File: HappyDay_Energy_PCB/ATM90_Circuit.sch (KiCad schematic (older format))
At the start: 34 parts

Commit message: sacrificial draft of power section / HappyDay Energy Monitor Schematic
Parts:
- added L? (x2): L_Core_Ferrite_Small, symbol L_Core_Ferrite_Small
- added U?: Si8655_QSOP-16, QSOP-16, symbol Si8655_QSOP-16
- C? (x10): PN (none) -> C
- C?: value C -> 18p; PN (none) -> c
- C? (x3): value C -> 18p; PN (none) -> C
- J? (x4): PN (none) -> X
- M? (x2): PN (none) -> ATM90E26-YU-RCT-ND
- Y? (x2): PN (none) -> 535-9865-1-ND
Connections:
- net labels added: 3.3V_AVDD, GNDA, GNDREF
- net labels removed: AGND
- wire segments 156 -> 173
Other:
- note added: "ATM90e26 Power"
- moved on the sheet: C?, Y?

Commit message: evolved schematic
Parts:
- removed U?: Si8655_QSOP-16, QSOP-16, symbol Si8655_QSOP-16
- added U?: Si8655, QSOP-16, symbol Si8655
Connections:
- net labels added: +3.3VA, 5V_UNREG, CS0_ATM, CS0_MCU, CS1_ATM, CS1_MCU, GNDPWR, MISO_ATM, MISO_MCU, MOSI_ATM, MOSI_MCU, SCLK_ATM, SCLK_MCU
- net labels removed: CS_0, CS_1, MISO, MOSI, SCLK
- wire segments 173 -> 187
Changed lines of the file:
@@
 	3500 4800 3200 4800
 Text GLabel 3500 4900 2    60   Input ~ 0
-CS_0
+CS0_ATM
 Wire Wire Line
 	3500 4900 3200 4900
@@
 	3500 4600 3200 4600
 Text GLabel 3500 4600 2    60   Input ~ 0
-MOSI
+MOSI_ATM
 Text GLabel 3500 4700 2    60   Output ~ 0
-MISO
+MISO_ATM
 Text GLabel 3500 4800 2    60   Input ~ 0
-SCLK
+SCLK_ATM
 $Comp
 L ATM90E26_ATM90E26 M?
@@
 	7550 4950 7250 4950
 Text GLabel 7550 5050 2    60   Input ~ 0
-CS_1
+CS1_ATM
 Wire Wire Line
 	7550 5050 7250 5050
@@
 	7550 4750 7250 4750
 Text GLabel 7550 4750 2    60   Input ~ 0
-MOSI
+MOSI_ATM
 Text GLabel 7550 4850 2    60   Output ~ 0
-MISO
+MISO_ATM
 Text GLabel 7550 4950 2    60   Input ~ 0
-SCLK
+SCLK_ATM
 $Comp
 L Crystal_Small Y?
@@
 $EndComp
 Text GLabel 10050 5700 3    60   Input ~ 0
-MISO
+MISO_MCU
 Wire Wire Line
 	10050 5700 10050 5500
 Text GLabel 9950 5700 3    60   Output ~ 0
-MOSI
+MOSI_MCU
 Wire Wire Line
 	9950 5500 9950 5700
 Text GLabel 9850 5700 3    60   Output ~ 0
-SCLK
+SCLK_MCU
 Wire Wire Line
 	9850 5700 9850 5500
@@
 Wire Wire Line
 	9250 4350 9250 4550
-$Comp
-L GNDD #PWR?
-U 1 1 5A131861
-P 9150 5700
-F 0 "#PWR?" H 9150 5450 50  0001 C CNN
-F 1 "GNDD" H 9150 5575 50  0000 C CNN
-F 2 "" H 9150 5700 50  0001 C CNN
-F 3 "" H 9150 5700 50  0001 C CNN
-	1    9150 5700
-	1    0    0    -1
-$EndComp
 Wire Wire Line
 	9150 5700 9150 5500
 Text GLabel 9650 4400 1    60   Output ~ 0
-CS_1
+CS1_MCU
 Wire Wire Line
 	9650 4400 9650 4550
 Text GLabel 9750 4400 1    60   Output ~ 0
-CS_0
+CS0_MCU
 Wire Wire Line
 	9750 4400 9750 4550
-$Comp
-L Si8655_QSOP-16 U?
-U 1 1 5A1484DC
-P 7200 1750
-F 0 "U?" H 7850 900 60  0000 C CNN
-F 1 "Si8655_QSOP-16" H 7850 1900 60  0000 C CNN
-F 2 "QSOP-16" H 8400 1990 60  0001 C CNN
-F 3 "" H 7200 1750 60  0000 C CNN
-	1    7200 1750
-	1    0    0    -1
-$EndComp
 Text HLabel 1050 1350 1    60   Input ~ 12
 3.3V_AVDD
@@
 Wire Wire Line
 	1050 1450 1050 1350
-$Comp
-L +3.3V #PWR?
-U 1 1 5A14FD34
-P 600 1250
-F 0 "#PWR?" H 600 1100 50  0001 C CNN
-F 1 "+3.3V" H 600 1390 50  0000 C CNN
-F 2 "" H 600 1250 50  0001 C CNN
-F 3 "" H 600 1250 50  0001 C CNN
-	1    600  1250
-	1    0    0    -1
-$EndComp
 Wire Wire Line
 	600  1250 600  1450
 Wire Wire Line
 	600  1450 700  1450
-$Comp
-L +3.3V #PWR?
-U 1 1 5A14FF70
-P 850 4200
-F 0 "#PWR?" H 850 4050 50  0001 C CNN
-F 1 "+3.3V" H 850 4340 50  0000 C CNN
-F 2 "" H 850 4200 50  0001 C CNN
-F 3 "" H 850 4200 50  0001 C CNN
-	1    850  4200
-	1    0    0    -1
-$EndComp
-$Comp
-L +3.3V #PWR?
-U 1 1 5A14FFE7
-P 2600 3650
-F 0 "#PWR?" H 2600 3500 50  0001 C CNN
-F 1 "+3.3V" H 2600 3790 50  0000 C CNN
-F 2 "" H 2600 3650 50  0001 C CNN
-F 3 "" H 2600 3650 50  0001 C CNN
-	1    2600 3650
-	1    0    0    -1
-$EndComp
-$Comp
-L +3.3V #PWR?
-U 1 1 5A150082
-P 6650 3750
-F 0 "#PWR?" H 6650 3600 50  0001 C CNN
-F 1 "+3.3V" H 6650 3890 50  0000 C CNN
-F 2 "" H 6650 3750 50  0001 C CNN
-F 3 "" H 6650 3750 50  0001 C CNN
-	1    6650 3750
-	1    0    0    -1
-$EndComp
-$Comp
-L +3.3V #PWR?
-U 1 1 5A15011D
-P 5000 4400
-F 0 "#PWR?" H 5000 4250 50  0001 C CNN
-F 1 "+3.3V" H 5000 4540 50  0000 C CNN
-F 2 "" H 5000 4400 50  0001 C CNN
-F 3 "" H 5000 4400 50  0001 C CNN
-	1    5000 4400
-	1    0    0    -1
-$EndComp
-$Comp
-L +3.3V #PWR?
-U 1 1 5A150290
-P 9250 4350
-F 0 "#PWR?" H 9250 4200 50  0001 C CNN
-F 1 "+3.3V" H 9250 4490 50  0000 C CNN
-F 2 "" H 9250 4350 50  0001 C CNN
-F 3 "" H 9250 4350 50  0001 C CNN
-	1    9250 4350
-	1    0    0    -1
-$EndComp
-$Comp
-L +3.3V #PWR?
-U 1 1 5A150532
-P 7050 1550
-F 0 "#PWR?" H 7050 1400 50  0001 C CNN
-F 1 "+3.3V" H 7050 1690 50  0000 C CNN
-F 2 "" H 7050 1550 50  0001 C CNN
-F 3 "" H 7050 1550 50  0001 C CNN
-	1    7050 1550
-	1    0    0    -1
-$EndComp
-Wire Wire Line
-	7200 1750 7050 1750
-Wire Wire Line
-	7050 1750 7050 1550
 $Comp
 L GNDD #PWR?
 U 1 1 5A150691
-P 7200 2600
-F 0 "#PWR?" H 7200 2350 50  0001 C CNN
-F 1 "GNDD" H 7200 2475 50  0000 C CNN
-F 2 "" H 7200 2600 50  0001 C CNN
-F 3 "" H 7200 2600 50  0001 C CNN
-	1    7200 2600
-	1    0    0    -1
-$EndComp
-Wire Wire Line
-	7200 2600 7200 2450
-Wire Wire Line
-	7200 1850 6050 1850
-Wire Wire Line
-	6050 1850 6050 2000
-$Comp
-L GNDD #PWR?
-U 1 1 5A1508DF
-P 6050 2000
-F 0 "#PWR?" H 6050 1750 50  0001 C CNN
-F 1 "GNDD" H 6050 1875 50  0000 C CNN
-F 2 "" H 6050 2000 50  0001 C CNN
-F 3 "" H 6050 2000 50  0001 C CNN
-	1    6050 2000
-	1    0    0    -1
-$EndComp
+P 9000 2600
+F 0 "#PWR?" H 9000 2350 50  0001 C CNN
+F 1 "GNDD" H 9000 2475 50  0000 C CNN
+F 2 "" H 9000 2600 50  0001 C CNN
+F 3 "" H 9000 2600 50  0001 C CNN
+	1    9000 2600
+	1    0    0    -1
+$EndComp
+Wire Wire Line
+	9000 2400 9000 2600
 Text HLabel 1750 1300 1    60   Input ~ 0
 GNDA
@@
 Wire Notes Line
 	2650 2450 2650 500
+Text GLabel 9150 1900 2    60   Output ~ 0
+SCLK_ATM
+Wire Wire Line
+	8850 1900 9150 1900
+Wire Wire Line
+	8850 1700 9000 1700
+Wire Wire Line
+	9000 1550 9000 1800
+Wire Wire Line
+	8850 2400 9000 2400
+Text GLabel 9150 2000 2    60   Output ~ 0
+MOSI_ATM
+Wire Wire Line
+	9150 2000 8850 2000
+Text GLabel 9150 2100 2    60   Output ~ 0
+CS0_ATM
+Wire Wire Line
+	9150 2100 8850 2100
+Text GLabel 9150 2200 2    60   Output ~ 0
+CS1_ATM
+Wire Wire Line
+	9150 2200 8850 2200
+Text GLabel 9150 2300 2    60   Input ~ 0
+MISO_ATM
+Wire Wire Line
+	9150 2300 8850 2300
+$Comp
+L Si8655 U?
+U 1 1 5A188915
+P 7450 1700
+F 0 "U?" H 8100 850 60  0000 C CNN
+F 1 "Si8655" H 8100 1850 60  0000 C CNN
+F 2 "QSOP-16" H 8650 1940 60  0001 C CNN
+F 3 "" H 7450 1700 60  0000 C CNN
+	1    7450 1700
+	1    0    0    -1
+$EndComp
+Wire Wire Line
+	9000 1800 8850 1800
+Connection ~ 9000 1700
+$Comp
+L +3.3VA #PWR?
+U 1 1 5A1892D8
+P 600 1250
+F 0 "#PWR?" H 600 1100 50  0001 C CNN
+F 1 "+3.3VA" H 600 1390 50  0000 C CNN
+F 2 "" H 600 1250 50  0001 C CNN
+F 3 "" H 600 1250 50  0001 C CNN
+	1    600  1250
+	1    0    0    -1
+$EndComp
+$Comp
+L +3.3VA #PWR?
+U 1 1 5A1893A5
+P 850 4200
+F 0 "#PWR?" H 850 4050 50  0001 C CNN
+F 1 "+3.3VA" H 850 4340 50  0000 C CNN
+F 2 "" H 850 4200 50  0001 C CNN
+F 3 "" H 850 4200 50  0001 C CNN
+	1    850  4200
+	1    0    0    -1
+$EndComp
+$Comp
+L +3.3VA #PWR?
+U 1 1 5A18941F
+P 2600 3650
+F 0 "#PWR?" H 2600 3500 50  0001 C CNN
+F 1 "+3.3VA" H 2600 3790 50  0000 C CNN
+F 2 "" H 2600 3650 50  0001 C CNN
+F 3 "" H 2600 3650 50  0001 C CNN
+	1    2600 3650
+	1    0    0    -1
+$EndComp
+$Comp
+L +3.3VA #PWR?
+U 1 1 5A189579
+P 6650 3750
+F 0 "#PWR?" H 6650 3600 50  0001 C CNN
+F 1 "+3.3VA" H 6650 3890 50  0000 C CNN
+F 2 "" H 6650 3750 50  0001 C CNN
+F 3 "" H 6650 3750 50  0001 C CNN
+	1    6650 3750
+	1    0    0    -1
+$EndComp
+$Comp
+L +3.3VA #PWR?
+U 1 1 5A1895F3
+P 5000 4400
+F 0 "#PWR?" H 5000 4250 50  0001 C CNN
+F 1 "+3.3VA" H 5000 4540 50  0000 C CNN
+F 2 "" H 5000 4400 50  0001 C CNN
+F 3 "" H 5000 4400 50  0001 C CNN
+	1    5000 4400
+	1    0    0    -1
+$EndComp
+$Comp
+L +3.3VA #PWR?
+U 1 1 5A18984F
+P 9000 1550
+F 0 "#PWR?" H 9000 1400 50  0001 C CNN
+F 1 "+3.3VA" H 9000 1690 50  0000 C CNN
+F 2 "" H 9000 1550 50  0001 C CNN
+F 3 "" H 9000 1550 50  0001 C CNN
+	1    9000 1550
+	1    0    0    -1
+$EndComp
+Text GLabel 7000 1900 0    60   Input ~ 0
+SCLK_MCU
+Wire Wire Line
+	7000 1900 7450 1900
+Text GLabel 7000 2000 0    60   Input ~ 0
+MOSI_MCU
+Wire Wire Line
+	7000 2000 7450 2000
+Text GLabel 6950 2300 0    60   Output ~ 0
+MISO_MCU
+Wire Wire Line
+	7450 2300 6950 2300
+Text GLabel 7000 2100 0    60   Input ~ 0
+CS0_MCU
+Text GLabel 7000 2200 0    60   Input ~ 0
+CS1_MCU
+Wire Wire Line
+	7450 2100 7000 2100
+Wire Wire Line
+	7450 2200 7000 2200
+Text HLabel 9150 5700 3    60   Input ~ 0
+GNDPWR
+Text HLabel 9250 4350 1    60   Input ~ 0
+5V_UNREG
+$Comp
+L +3.3V #PWR?
+U 1 1 5A18B898
+P 8950 5700
+F 0 "#PWR?" H 8950 5550 50  0001 C CNN
+F 1 "+3.3V" H 8950 5840 50  0000 C CNN
+F 2 "" H 8950 5700 50  0001 C CNN
+F 3 "" H 8950 5700 50  0001 C CNN
+	1    8950 5700
+	-1   0    0    1
+$EndComp
+Wire Wire Line
+	8950 5700 8950 5500
+$Comp
+L +3.3V #PWR?
+U 1 1 5A18BDB9
+P 7400 1600
+F 0 "#PWR?" H 7400 1450 50  0001 C CNN
+F 1 "+3.3V" H 7400 1740 50  0000 C CNN
+F 2 "" H 7400 1600 50  0001 C CNN
+F 3 "" H 7400 1600 50  0001 C CNN
+	1    7400 1600
+	1    0    0    -1
+$EndComp
+Wire Wire Line
+	7450 1700 7400 1700
+Wire Wire Line
+	7400 1700 7400 1600
+Text HLabel 6950 1800 0    60   Input ~ 0
+GNDPWR
+Wire Wire Line
+	7450 1800 6950 1800
 $EndSCHEMATC

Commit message: evolved schematic
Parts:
- removed U?: Si8655, QSOP-16, symbol Si8655
- added .1u1, .1u2: C, symbol C
- added R14, R15, R16, R17, R18, R19, R20, R21, R22, R23: 50, symbol R
- added U4: Si8655, QSOP-16, symbol Si8655
- gave numbers to parts that had none: 36
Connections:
- net +3.3VA: now also .1u2.1, U4.10 (EN2), U4.16 (VDD2)
- net +3V3: now also .1u1.1, U4.1 (VDD1)
- net CS0_ATM: now also R21.1
- net CS0_MCU: now also R16.2
- net CS1_ATM: now also R22.1
- net CS1_MCU: now also R17.2
- net GNDD: now also .1u2.2, U4.9 (GND2)
- net MISO_ATM: now also R23.1
- net MISO_MCU: now also R18.2
- net MOSI_ATM: now also R20.1
- net MOSI_MCU: now also R15.2
- net SCLK_ATM: now also R19.1
- net SCLK_MCU: now also R14.2
- net 5V_UNREG renamed 5V_UNREG_D
- net GNDPWR renamed GND_D
- net GND_D: now also .1u1.2, U4.8 (GND1)
- new net: R14.1, U4.2 (A1)
- new net: R15.1, U4.3 (A2)
- new net: R16.1, U4.4 (A3)
- new net: R17.1, U4.5 (A4)
- new net: R18.1, U4.6 (A5)
- new net: R19.2, U4.15 (B1)
- new net: R20.2, U4.14 (B2)
- new net: R21.2, U4.13 (B3)
- new net: R22.2, U4.12 (B4)
- new net: R23.2, U4.11 (B5)

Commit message: evolved layout
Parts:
- removed J12: ZX1_TP, symbol TEST_1P
- removed J13: IRQ1_TP, symbol TEST_1P
- removed J14: CF21_TP, symbol TEST_1P
- removed J15: CF11_TP, symbol TEST_1P
- removed J16: WARN1_TP, symbol TEST_1P
- removed J19: Conn_01x16, symbol Conn_01x16
- removed J20: Conn_01x12, symbol Conn_01x12
- removed J5: ZX0_TP, symbol TEST_1P
- removed J6: IRQ0_TP, symbol TEST_1P
- removed J7: CF20_TP, symbol TEST_1P
- removed J8: CF10_TP, symbol TEST_1P
- removed J9: WARN0_TP, symbol TEST_1P
- removed U4: Si8655, QSOP-16, symbol Si8655
- added C22: .1u, Capacitors_SMD:C_0805_HandSoldering, symbol C
- added R24: 10K, Capacitors_SMD:C_0805_HandSoldering, symbol R
- added U3: Si865, HappyDayEnergyMonitor:Si865, symbol Si8655
- added U4: FeatherHuzzah, HappyDayEnergyMonitor:ADAFRUIT_FEATHER, symbol FeatherHuzzah
- C10, C11, C12, C13, C14, C15, C16, C17, C18, C19, C20, C21, C8, C9: footprint (none) -> Capacitors_SMD:C_0805_HandSoldering
- C6: renamed from .1u1; value C -> .1u; footprint (none) -> Capacitors_SMD:C_0805_HandSoldering; PN (none) -> C
- C7: renamed from .1u2; value C -> .1u; footprint (none) -> Capacitors_SMD:C_0805_HandSoldering; PN (none) -> C
- L2: footprint (none) -> Capacitors_SMD:C_0805_HandSoldering; PN (none) -> MH2029-601Y
- L3: footprint (none) -> Capacitors_SMD:C_0805_HandSoldering; PN (none) -> BLM15AG100SN1D
- M1, M2: footprint (none) -> HappyDayEnergyMonitor:SSOP-28_5.3x10.2mm_Pitch0.65mm; PN ATM90E26-YU-RCT-ND -> (none)
- R14, R15, R16, R17, R18, R19, R20, R21, R22, R23: value 50 -> 51; footprint (none) -> Resistors_SMD:R_0805_HandSoldering; PN (none) -> R
- Y1, Y2: footprint (none) -> HappyDayEnergyMonitor:Crystal
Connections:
- net +3.3VA: now also U3.10 (EN2), U3.16 (VDD2)
- net +3V3: now also R24.2, U3.1 (VDD1), U4.15 (3V3)
- net CS0_ATM: now also R20.1; no longer R21.1
- net CS0_MCU: now also R15.1, R15.2, U3.3 (A2), U4.23 (CS1); no longer R16.2
- net CS1_ATM: now also R19.1; no longer R22.1
- net CS1_MCU: now also R14.1, R14.2, U3.2 (A1), U4.24 (CS0); no longer R17.2
- net GNDD: now also U3.9 (GND2); no longer C19.2, C21.2, M2.14 (AGND)
- net MISO_MCU: now also R18.1, U3.6 (A5), U4.4 (MISO)
- net MOSI_ATM: now also R21.1; no longer R20.1
- net MOSI_MCU: now also R16.1, R16.2, U3.4 (A3), U4.5 (MOSI); no longer R15.2
- net SCLK_ATM: now also R22.1; no longer R19.1
- net SCLK_MCU: now also R17.2, U4.6 (SCK); no longer R14.2
- net SCK_MCU: now reaches R17.1
- net SCK_MCU: now also U3.5 (A4)
- net at R19.2: now also U3.15 (B1)
- net at R20.2: now also U3.14 (B2)
- net at R21.2: now also U3.13 (B3)
- net at R22.2: now also U3.12 (B4)
- net at R23.2: now also U3.11 (B5)
- net CF1_0: no longer names the net of M1.18 (CF1)
- net CF1_1: no longer names the net of M2.18 (CF1)
- net CF2_0: no longer names the net of M1.19 (CF2)
- net CF2_1: no longer names the net of M2.19 (CF2)
- net GND_D renamed GND_MCU
- net GND_MCU: now also C22.2, U3.8 (GND1), U4.13 (GND)
- net IRQ_0: no longer names the net of M1.20 (IRQ)
- net IRQ_1: no longer names the net of M2.20 (IRQ)
- net WARN_0: no longer names the net of M1.17 (WARNOUT)
- net WARN_1: no longer names the net of M2.17 (WARNOUT)
- net ZX_0: no longer names the net of M1.21 (ZX)
- net ZX_1: no longer names the net of M2.21 (ZX)
- new net: C19.2, C21.2, M2.14 (AGND)
- new net: R24.1, U4.18 (EN)
- new net 3.3V_MCU: C22.1, U4.17 (BAT)
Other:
- moved on the sheet: C7

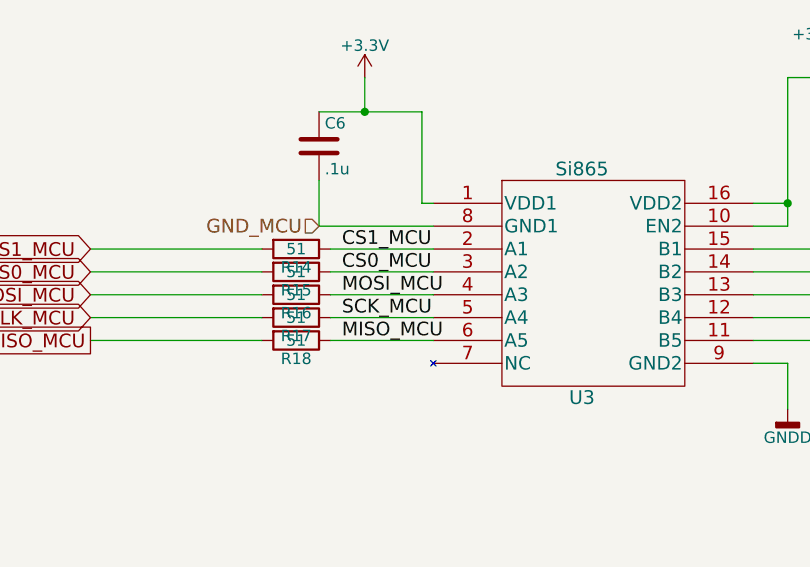
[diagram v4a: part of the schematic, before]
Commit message: Kicad PCB sent to OSH Park
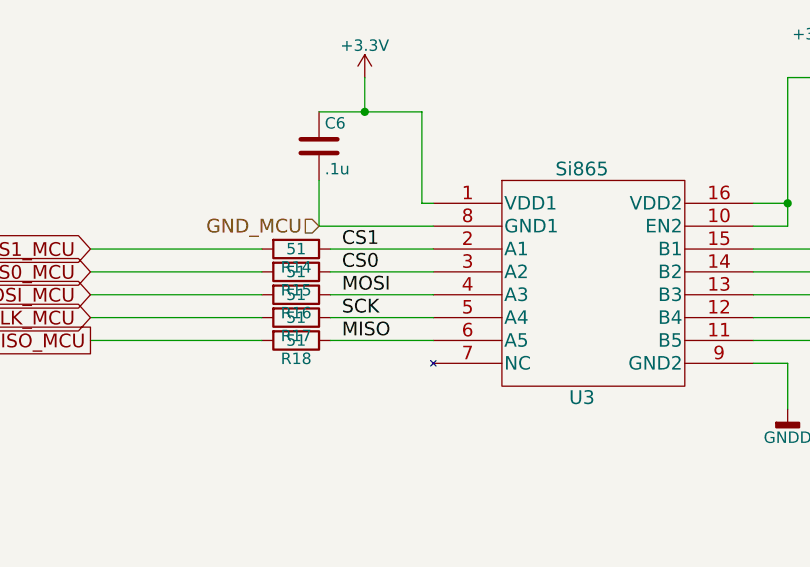
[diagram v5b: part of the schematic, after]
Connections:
- net CS0_MCU: no longer R15.1, U3.3 (A2)
- net CS1_MCU: no longer R14.1, U3.2 (A1)
- net MISO_MCU: no longer R18.1, U3.6 (A5)
- net MOSI_MCU: no longer R16.1, U3.4 (A3)
- net SCK_MCU renamed SCK
- new net CS0: R15.1, U3.3 (A2)
- new net CS1: R14.1, U3.2 (A1)
- new net MISO: R18.1, U3.6 (A5)
- new net MOSI: R16.1, U3.4 (A3)
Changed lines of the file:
@@
 $EndComp
 Text Label 7050 2200 0    60   ~ 0
-SCK_MCU
+SCK
 Text Label 7050 2100 0    60   ~ 0
-MOSI_MCU
+MOSI
 Text Label 7050 2000 0    60   ~ 0
-CS0_MCU
+CS0
 Text Label 7050 1900 0    60   ~ 0
-CS1_MCU
+CS1
 Text Label 7050 2300 0    60   ~ 0
-MISO_MCU
+MISO
 Wire Wire Line
 	6700 2000 5950 2000

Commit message: files sent to OSH Park for sacrificial draft build
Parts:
- C13: PN c -> C
- M1, M2: PN (none) -> ATM90E26-YU-B
- U4: PN (none) -> x
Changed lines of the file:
@@
 F 2 "Capacitors_SMD:C_0805_HandSoldering" H 3388 2100 50  0001 C CNN
 F 3 "" H 3350 2250 50  0001 C CNN
-F 4 "c" H 3350 2250 60  0001 C CNN "PN"
+F 4 "C" H 3350 2250 60  0001 C CNN "PN"
 	1    3350 2250
 	1    0    0    -1
@@
 F 2 "HappyDayEnergyMonitor:ADAFRUIT_FEATHER" H 11000 4300 60  0001 C CNN
 F 3 "" H 11000 4300 60  0001 C CNN
+F 4 "x" H 11000 4300 60  0001 C CNN "PN"
 	2    11000 4300
 	0    -1   -1   0
@@
 F 2 "HappyDayEnergyMonitor:SSOP-28_5.3x10.2mm_Pitch0.65mm" H 6650 5350 60  0001 C CNN
 F 3 "" H 6650 5350 60  0001 C CNN
+F 4 "ATM90E26-YU-B" H 6650 5350 60  0001 C CNN "PN"
 	1    6650 5350
 	1    0    0    -1
@@
 F 2 "HappyDayEnergyMonitor:SSOP-28_5.3x10.2mm_Pitch0.65mm" H 2600 5200 60  0001 C CNN
 F 3 "" H 2600 5200 60  0001 C CNN
+F 4 "ATM90E26-YU-B" H 2600 5200 60  0001 C CNN "PN"
 	1    2600 5200
 	1    0    0    -1

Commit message: updates, particularly to layout - but not finished
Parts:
- C10, C11, C12, C17, C18, C19, C20, C21, C22, C6, C7, C8, C9, L2, R24: footprint Capacitors_SMD:C_0805_HandSoldering -> Capacitors_SMD:C_0805
- C13, C14, C15, C16: value 18p -> 27p; footprint Capacitors_SMD:C_0805_HandSoldering -> Capacitors_SMD:C_0805
- L3: footprint Capacitors_SMD:C_0805_HandSoldering -> Capacitors_SMD:C_0805; PN BLM15AG100SN1D -> MH2029-601Y
- M1, M2: symbol ATM90E26_ATM90E26 -> ATM90E26_ATM90E26-RESCUE-HappyDay_Energy_PCB
- R14, R15, R16, R17, R18, R19, R20, R21, R22, R23: footprint Resistors_SMD:R_0805_HandSoldering -> Capacitors_SMD:C_0805
- Y1, Y2: PN 535-9865-1-ND -> ABLS2-3.579545MHZ-D4Y-T
